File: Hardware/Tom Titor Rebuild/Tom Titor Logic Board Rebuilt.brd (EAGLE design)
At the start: 167.6 x 43.4 mm, 38 parts, among them J2 KLDX-0202-B, SW1 FSMRA4JH, SW2 FSMRA4JH, SW3 102-1261-EV, U1 LM7805CT, U2 1364-HVPS-H, U3 PIC16F628A, U4 DS1307+, U5 DS3232SN, X1 CRYSTAL, X2 32.768kHz

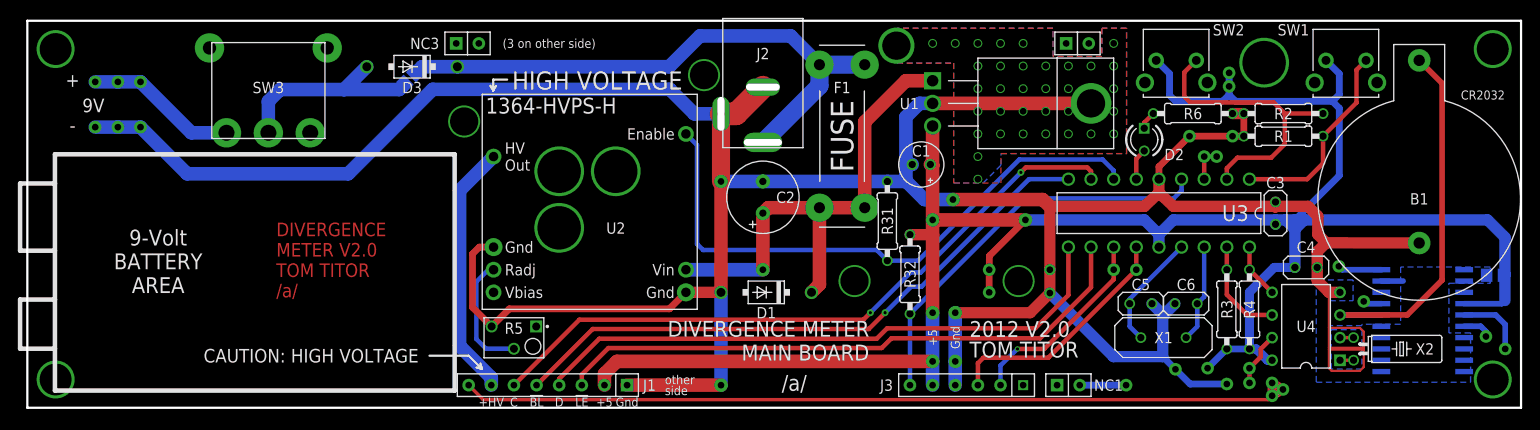
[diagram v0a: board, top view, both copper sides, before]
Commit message: Library mismatch fix
Major errors involved with a late change that was made to the component library. Don't let your layout and schematic get out of sync kids.
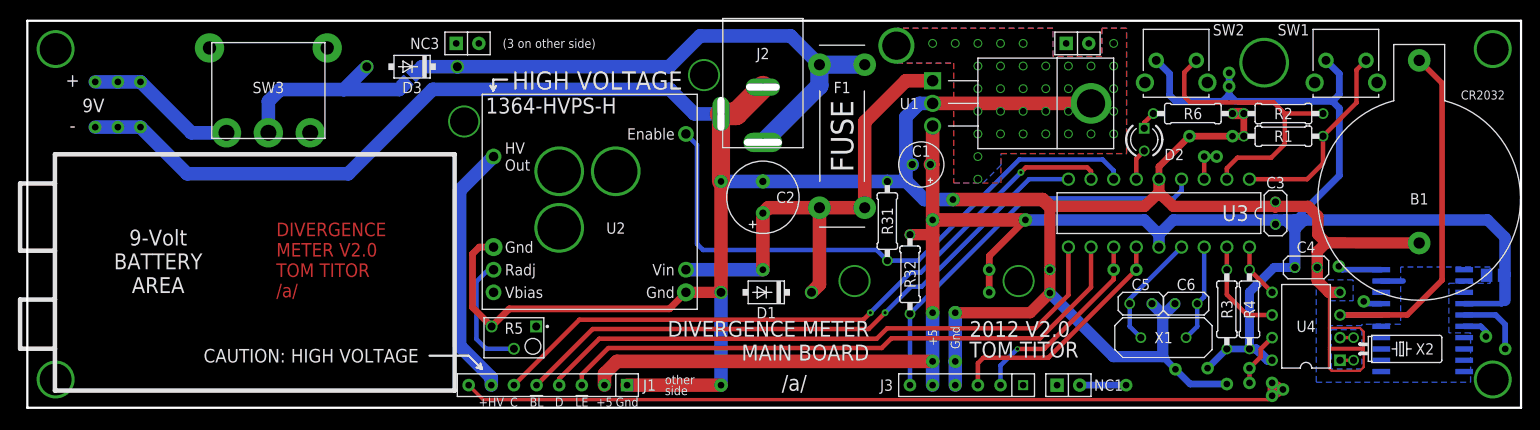
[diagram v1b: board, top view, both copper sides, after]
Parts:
- C1: value 33μF -> 33µF
- F1: device My Imported Components:5X20MM_FUSE -> My Imported Components:5X20MM
- J3: device My Imported Components:MA06-1 -> My Imported Components:MA06
